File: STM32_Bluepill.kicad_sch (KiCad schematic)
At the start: 28 parts, among them J1 USB_B_Micro, J2 Conn_01x04_Male, J3 Conn_01x04_Male, J4 Conn_01x04_Male, U1 STM32F103C8T6, U2 AMS1117-3.3, Y1 16MHz

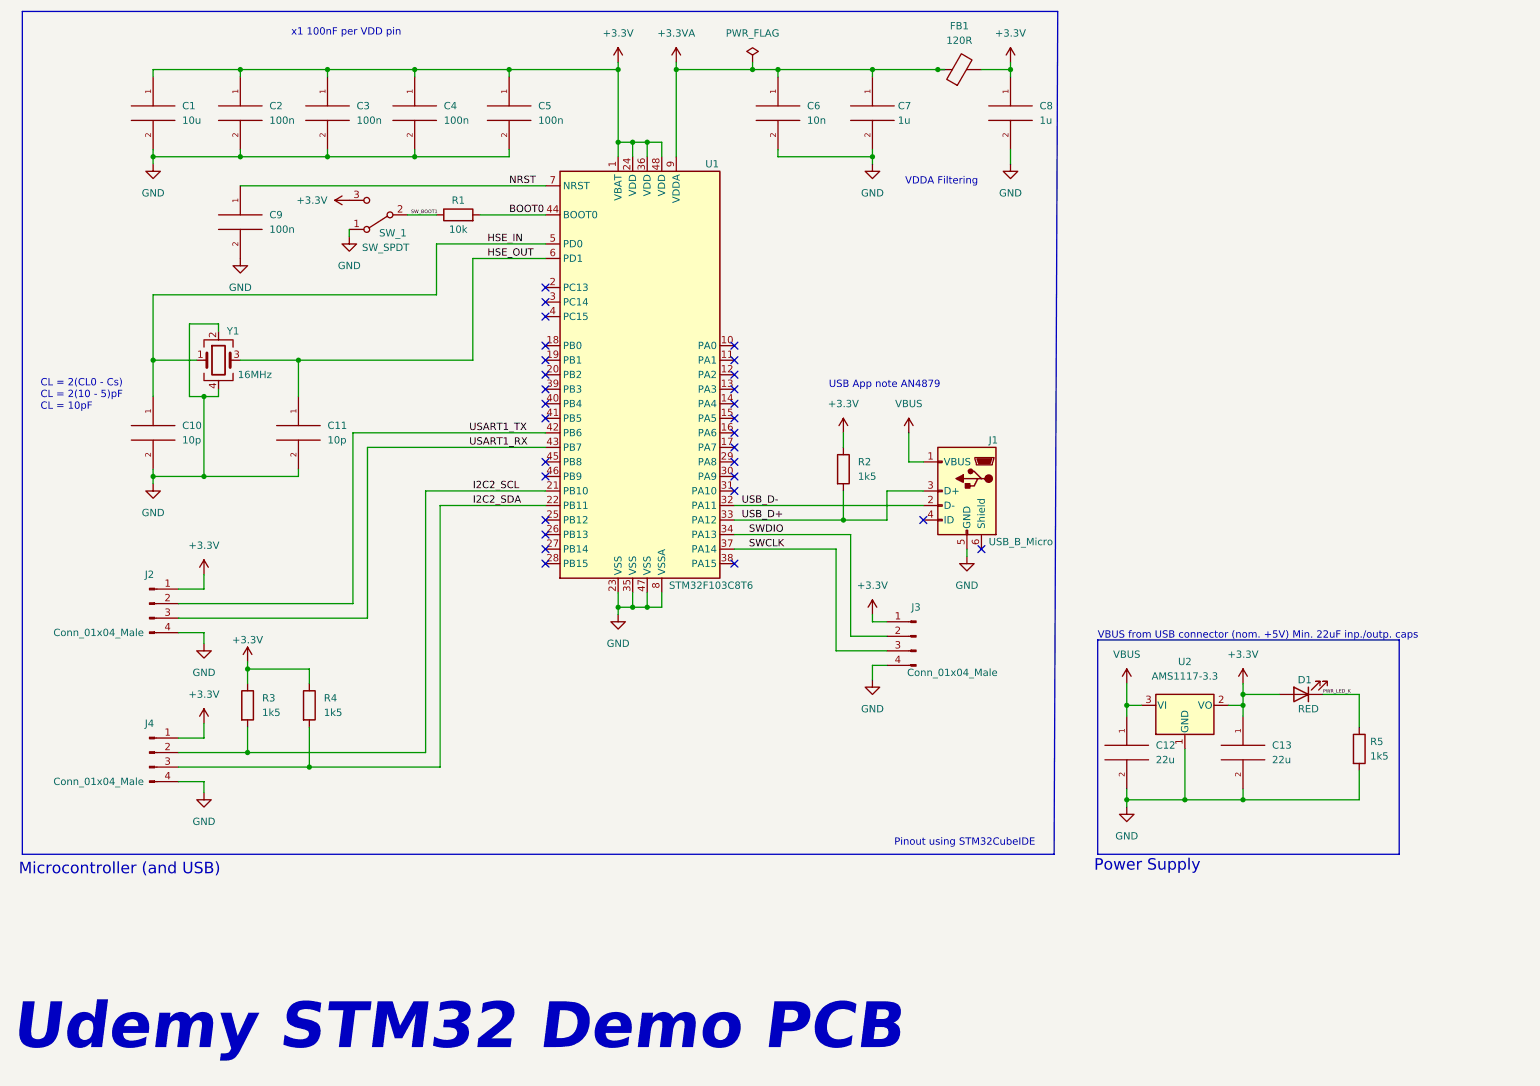
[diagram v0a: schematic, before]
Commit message: Schematic: Add M2 mounting holes
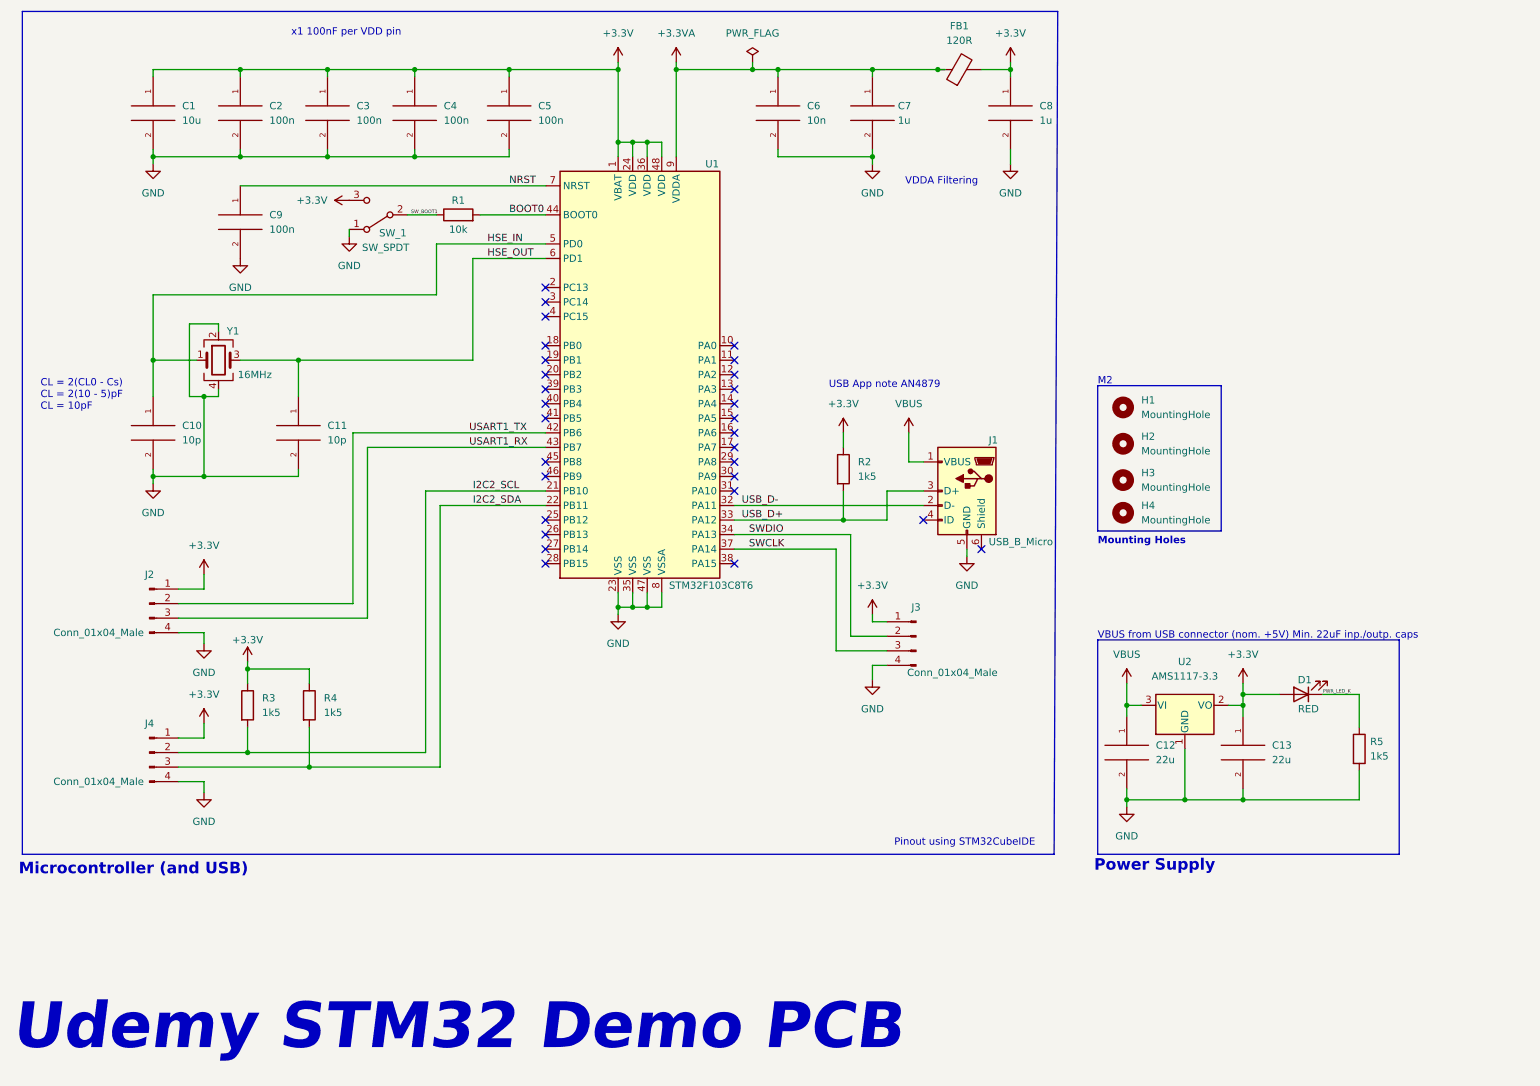
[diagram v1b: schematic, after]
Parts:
- added H1, H2, H3, H4: MountingHole, MountingHole:MountingHole_2.2mm_M2, symbol Mechanical:MountingHole
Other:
- note added: "M2"
- note added: "Mounting Holes"
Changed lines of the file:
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@@
+    (stroke (width 0) (type default) (color 0 0 0 0))
+  )
+  (polyline (pts (xy 202.565 80.01) (xy 224.155 80.01))
     (stroke (width 0) (type default) (color 0 0 0 0))
   )
@@
     (stroke (width 0) (type default) (color 0 0 0 0))
   )
+  (polyline (pts (xy 202.565 80.01) (xy 202.565 105.41))
+    (stroke (width 0) (type default) (color 0 0 0 0))
+  )
   (wire (pts (xy 43.815 69.215) (xy 43.815 81.915))
     (stroke (width 0) (type default) (color 0 0 0 0))
@@
     (stroke (width 0) (type default) (color 0 0 0 0))
   )
+  (polyline (pts (xy 224.155 80.01) (xy 224.155 105.41))
+    (stroke (width 0) (type default) (color 0 0 0 0))
+  )
   (wire (pts (xy 41.91 115.57) (xy 46.355 115.57))
     (stroke (width 0) (type default) (color 0 0 0 0))
   )
+  (polyline (pts (xy 224.155 105.41) (xy 202.565 105.41))
+    (stroke (width 0) (type default) (color 0 0 0 0))
+  )
   (wire (pts (xy 52.705 75.565) (xy 62.865 75.565))
     (stroke (width 0) (type default) (color 0 0 0 0))
@@
   )
   (text "Microcontroller (and USB)" (at 13.97 165.735 0)
-    (effects (font (size 2 2)) (justify left bottom))
+    (effects (font (size 2 2) (thickness 0.4) bold) (justify left bottom))
+  )
+  (text "M2" (at 202.565 80.01 0)
+    (effects (font (size 1.27 1.27)) (justify left bottom))
   )
   (text "Pinout using STM32CubeIDE" (at 167.005 160.655 0)
@@
   (text "CL = 2(CL0 - Cs)\nCL = 2(10 - 5)pF\nCL = 10pF" (at 17.78 84.455 0)
     (effects (font (size 1.27 1.27)) (justify left bottom))
+  )
+  (text "Mounting Holes" (at 202.565 107.95 0)
+    (effects (font (size 1.27 1.27) (thickness 0.254) bold) (justify left bottom))
   )
   (text "x1 100nF per VDD pin" (at 61.595 19.05 0)
@@
   )
   (text "Power Supply" (at 201.93 165.1 0)
-    (effects (font (size 2 2)) (justify left bottom))
+    (effects (font (size 2 2) (thickness 0.4) bold) (justify left bottom))
   )
   (label "USART1_TX" (at 92.71 88.265 0)
@@
     )
     (pin "1")
+  )
+  (symbol (lib_id "Mechanical:MountingHole") (at 207.01 96.52 0) (unit 1)
+    (in_bom yes) (on_board yes) (fields_autoplaced)
+    (property "Reference" "H3" (id 0) (at 210.185 95.2499 0)
+      (effects (font (size 1.27 1.27)) (justify left))
+    )
+    (property "Value" "MountingHole" (id 1) (at 210.185 97.7899 0)
+      (effects (font (size 1.27 1.27)) (justify left))
+    )
+    (property "Footprint" "MountingHole:MountingHole_2.2mm_M2" (id 2) (at 207.01 96.52 0)
+      (effects (font (size 1.27 1.27)) hide)
+    )
+    (property "Datasheet" "~" (id 3) (at 207.01 96.52 0)
+      (effects (font (size 1.27 1.27)) hide)
+    )
   )
   (symbol (lib_id "power:PWR_FLAG") (at 142.24 23.495 0) (unit 1)
@@
     (pin "1")
   )
+  (symbol (lib_id "Mechanical:MountingHole") (at 207.01 102.235 0) (unit 1)
+    (in_bom yes) (on_board yes) (fields_autoplaced)
+    (property "Reference" "H4" (id 0) (at 210.185 100.9649 0)
+      (effects (font (size 1.27 1.27)) (justify left))
+    )
+    (property "Value" "MountingHole" (id 1) (at 210.185 103.5049 0)
+      (effects (font (size 1.27 1.27)) (justify left))
+    )
+    (property "Footprint" "MountingHole:MountingHole_2.2mm_M2" (id 2) (at 207.01 102.235 0)
+      (effects (font (size 1.27 1.27)) hide)
+    )
+    (property "Datasheet" "~" (id 3) (at 207.01 102.235 0)
+      (effects (font (size 1.27 1.27)) hide)
+    )
+  )
   (symbol (lib_id "power:GND") (at 37.465 97.155 0) (unit 1)
     (in_bom yes) (on_board yes) (fields_autoplaced)
@@
     (pin "1")
   )
+  (symbol (lib_id "Mechanical:MountingHole") (at 207.01 90.17 0) (unit 1)
+    (in_bom yes) (on_board yes) (fields_autoplaced)
+    (property "Reference" "H2" (id 0) (at 210.185 88.8999 0)
+      (effects (font (size 1.27 1.27)) (justify left))
+    )
+    (property "Value" "MountingHole" (id 1) (at 210.185 91.4399 0)
+      (effects (font (size 1.27 1.27)) (justify left))
+    )
+    (property "Footprint" "MountingHole:MountingHole_2.2mm_M2" (id 2) (at 207.01 90.17 0)
+      (effects (font (size 1.27 1.27)) hide)
+    )
+    (property "Datasheet" "~" (id 3) (at 207.01 90.17 0)
+      (effects (font (size 1.27 1.27)) hide)
+    )
+  )
   (symbol (lib_id "pspice:C") (at 163.195 32.385 0) (unit 1)
     (in_bom yes) (on_board yes) (fields_autoplaced)
@@
     (pin "3")
     (pin "4")
+  )
+  (symbol (lib_id "Mechanical:MountingHole") (at 207.01 83.82 0) (unit 1)
+    (in_bom yes) (on_board yes) (fields_autoplaced)
+    (property "Reference" "H1" (id 0) (at 210.185 82.5499 0)
+      (effects (font (size 1.27 1.27)) (justify left))
+    )
+    (property "Value" "MountingHole" (id 1) (at 210.185 85.0899 0)
+      (effects (font (size 1.27 1.27)) (justify left))
+    )
+    (property "Footprint" "MountingHole:MountingHole_2.2mm_M2" (id 2) (at 207.01 83.82 0)
+      (effects (font (size 1.27 1.27)) hide)
+    )
+    (property "Datasheet" "~" (id 3) (at 207.01 83.82 0)
+      (effects (font (size 1.27 1.27)) hide)
+    )
   )
   (symbol (lib_id "Device:R") (at 53.975 135.89 0) (unit 1)
@@
       (reference "FB1") (unit 1) (value "120R") (footprint "Inductor_SMD:L_0603_1608Metric")
     )
+    (path "/c9875b29-a88f-4f16-988d-72417d6b90d6"
+      (reference "H1") (unit 1) (value "MountingHole") (footprint "MountingHole:MountingHole_2.2mm_M2")
+    )
+    (path "/bee84a10-75db-42be-a3b6-21e87aecc56f"
+      (reference "H2") (unit 1) (value "MountingHole") (footprint "MountingHole:MountingHole_2.2mm_M2")
+    )
+    (path "/067fb58a-8fc3-431c-b590-7ab581fac75d"
+      (reference "H3") (unit 1) (value "MountingHole") (footprint "MountingHole:MountingHole_2.2mm_M2")
+    )
+    (path "/6b480f17-9eba-427c-8354-bb2033009d88"
+      (reference "H4") (unit 1) (value "MountingHole") (footprint "MountingHole:MountingHole_2.2mm_M2")
+    )
     (path "/9f1c510e-32d3-4302-89a0-0925ff949f4e"

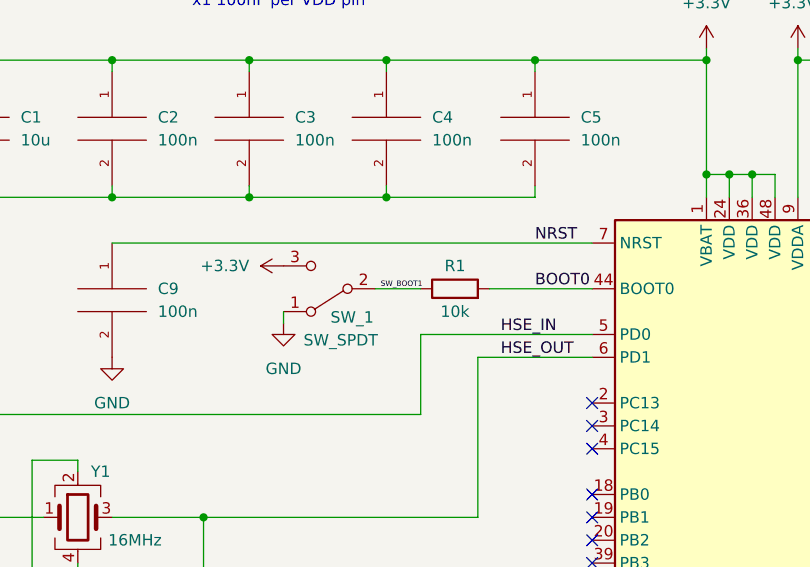
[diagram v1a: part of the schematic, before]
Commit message: Schematic/Layout: Rename SW_BOOT1 to SW_BOOT0 for net name
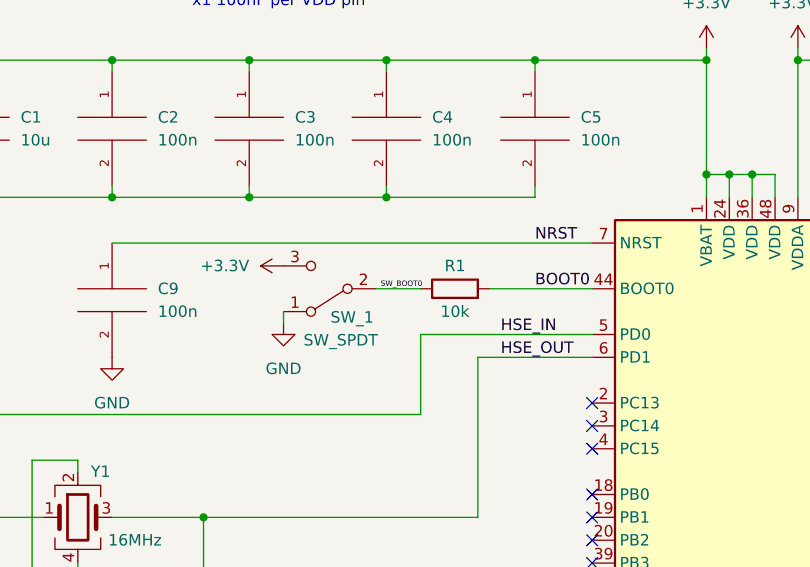
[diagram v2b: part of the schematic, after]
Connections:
- net SW_BOOT1 renamed SW_BOOT0
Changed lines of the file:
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@@
     (effects (font (size 1.27 1.27)) (justify left bottom))
   )
-  (label "SW_BOOT1" (at 82.55 50.165 0)
+  (label "SW_BOOT0" (at 82.55 50.165 0)
     (effects (font (size 0.6 0.6)) (justify left bottom))
   )
